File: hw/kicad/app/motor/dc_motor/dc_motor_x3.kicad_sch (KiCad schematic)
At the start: 23 parts, among them J1 TOP, J2 Motor 1, J3 Motor 2, J4 Motor 3, J6 BOTTUM, U1 DRV8870DDA, U2 DRV8870DDA, U3 DRV8870DDA

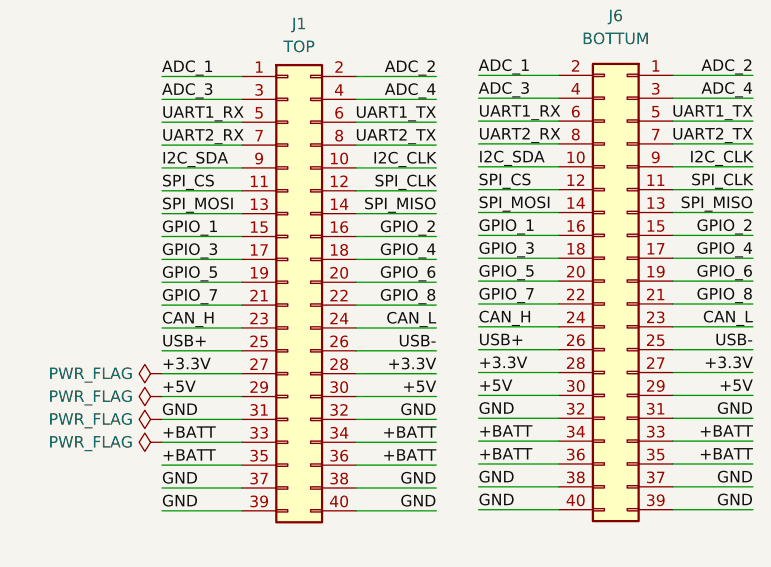
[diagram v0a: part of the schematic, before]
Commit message: 更换接口线序
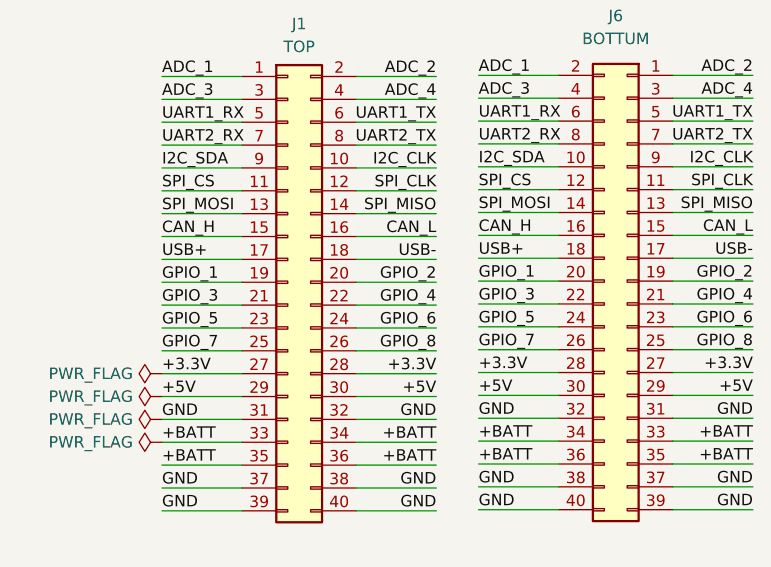
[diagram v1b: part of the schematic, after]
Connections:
- net CAN_H: now also J1.15 (Pin_15), J6.16 (Pin_16); no longer J1.23 (Pin_23), J6.24 (Pin_24)
- net CAN_L: now also J1.16 (Pin_16), J6.15 (Pin_15); no longer J1.24 (Pin_24), J6.23 (Pin_23)
- net ENC_1B: now also J1.25 (Pin_25), J6.26 (Pin_26); no longer J1.21 (Pin_21), J6.22 (Pin_22)
- net ENC_2B: now also J1.26 (Pin_26), J6.25 (Pin_25); no longer J1.22 (Pin_22), J6.21 (Pin_21)
- net GPIO_1: now also J1.19 (Pin_19), J6.20 (Pin_20); no longer J1.15 (Pin_15), J6.16 (Pin_16)
- net GPIO_2: now also J1.20 (Pin_20), J6.19 (Pin_19); no longer J1.16 (Pin_16), J6.15 (Pin_15)
- net GPIO_3: now also J1.21 (Pin_21), J6.22 (Pin_22); no longer J1.17 (Pin_17), J6.18 (Pin_18)
- net GPIO_4: now also J1.22 (Pin_22), J6.21 (Pin_21); no longer J1.18 (Pin_18), J6.17 (Pin_17)
- net GPIO_5: now also J1.23 (Pin_23), J6.24 (Pin_24); no longer J1.19 (Pin_19), J6.20 (Pin_20)
- net GPIO_6: now also J1.24 (Pin_24), J6.23 (Pin_23); no longer J1.20 (Pin_20), J6.19 (Pin_19)
- net USB+: now also J1.17 (Pin_17), J6.18 (Pin_18); no longer J1.25 (Pin_25), J6.26 (Pin_26)
- net USB-: now also J1.18 (Pin_18), J6.17 (Pin_17); no longer J1.26 (Pin_26), J6.25 (Pin_25)
